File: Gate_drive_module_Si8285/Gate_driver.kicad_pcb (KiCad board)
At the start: 2 copper layers, 33 parts, among them J1 CONN_01X10, J2 CONN_01X04, J3 CONN_01X03, J4 CONN_01X03, J5 CONN_01X03, U1 Si8285, U2 Mornsun_QA01C

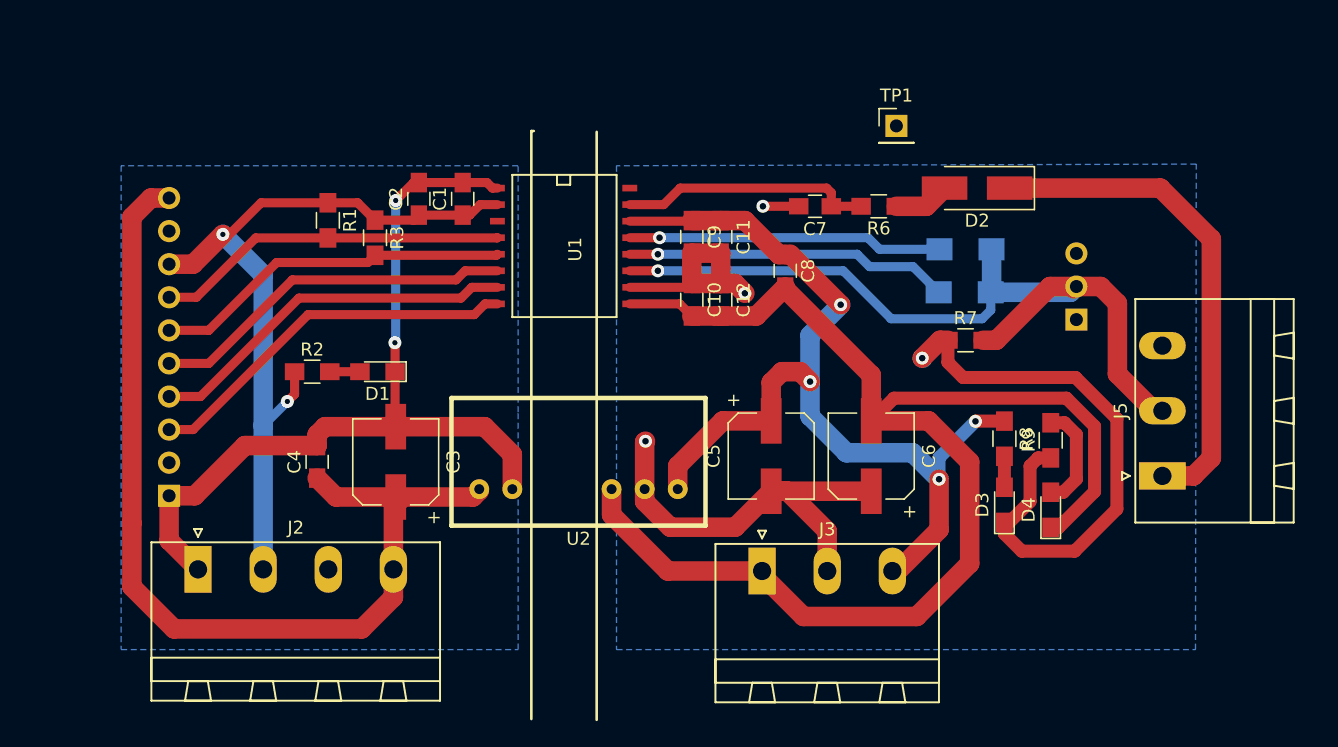
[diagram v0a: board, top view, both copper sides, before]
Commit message: Added edge cuts, logo, mounting holes, dimmensions, silkscreen
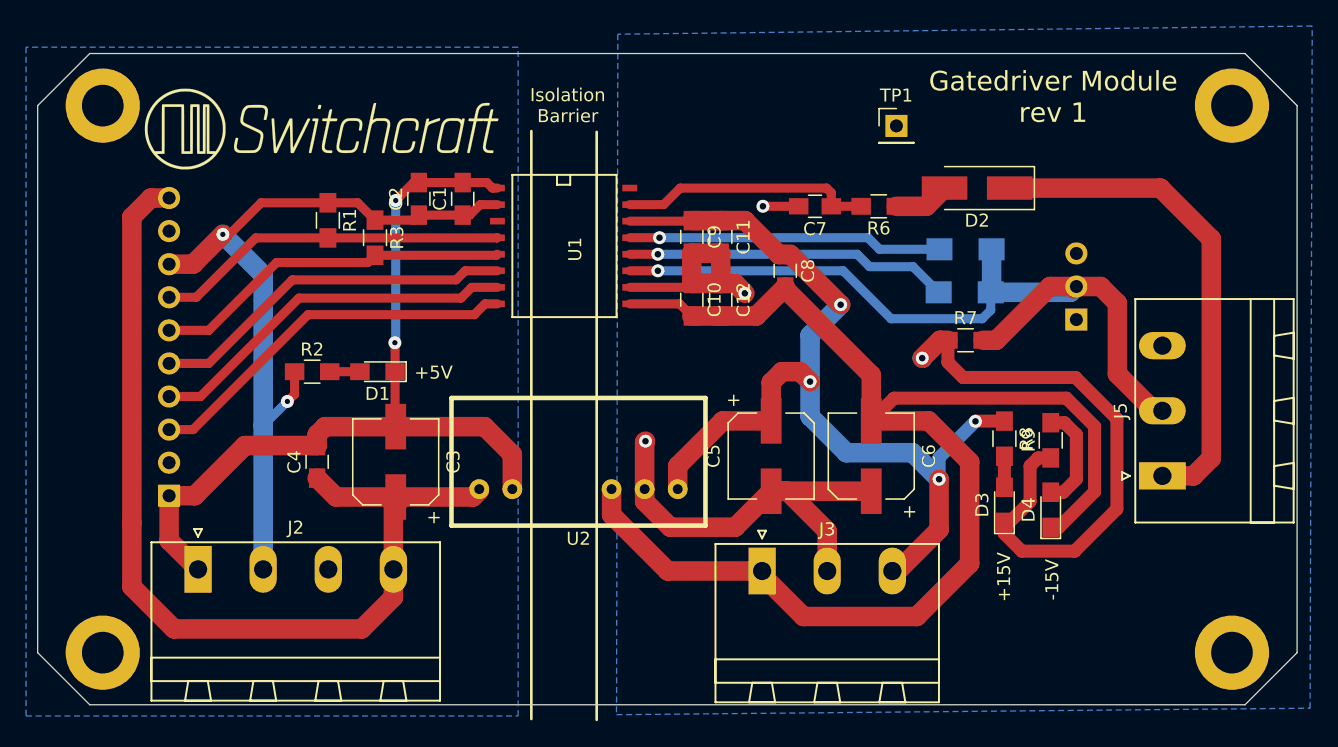
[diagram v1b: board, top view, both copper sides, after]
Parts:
- added G***: LOGO, Switchcraft:Switchcraft_medium_logo, F.Cu at (117.0, 111.8)
- added REF**: MountingHole_3.2mm_M3_ISO7380_Pad, Mounting_Holes:MountingHole_3.2mm_M3_ISO7380_Pad, F.Cu at (100.0, 110.0)
- added REF**: MountingHole_3.2mm_M3_ISO7380_Pad, Mounting_Holes:MountingHole_3.2mm_M3_ISO7380_Pad, F.Cu at (100.0, 152.0)
- added REF**: MountingHole_3.2mm_M3_ISO7380_Pad, Mounting_Holes:MountingHole_3.2mm_M3_ISO7380_Pad, F.Cu at (186.7, 110.0)
- added REF**: MountingHole_3.2mm_M3_ISO7380_Pad, Mounting_Holes:MountingHole_3.2mm_M3_ISO7380_Pad, F.Cu at (186.7, 152.0)
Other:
- board outline added: 96.7 x 50 mm
- board text added: "+15V"
- board text added: "+5V"
- board text added: "-15V"
- board text added: "Gatedriver Module rev 1"
- board text added: "Isolation Barrier"
- board text added: "Thou shall not pass"

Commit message: Added more measurements, adjusting screw holes
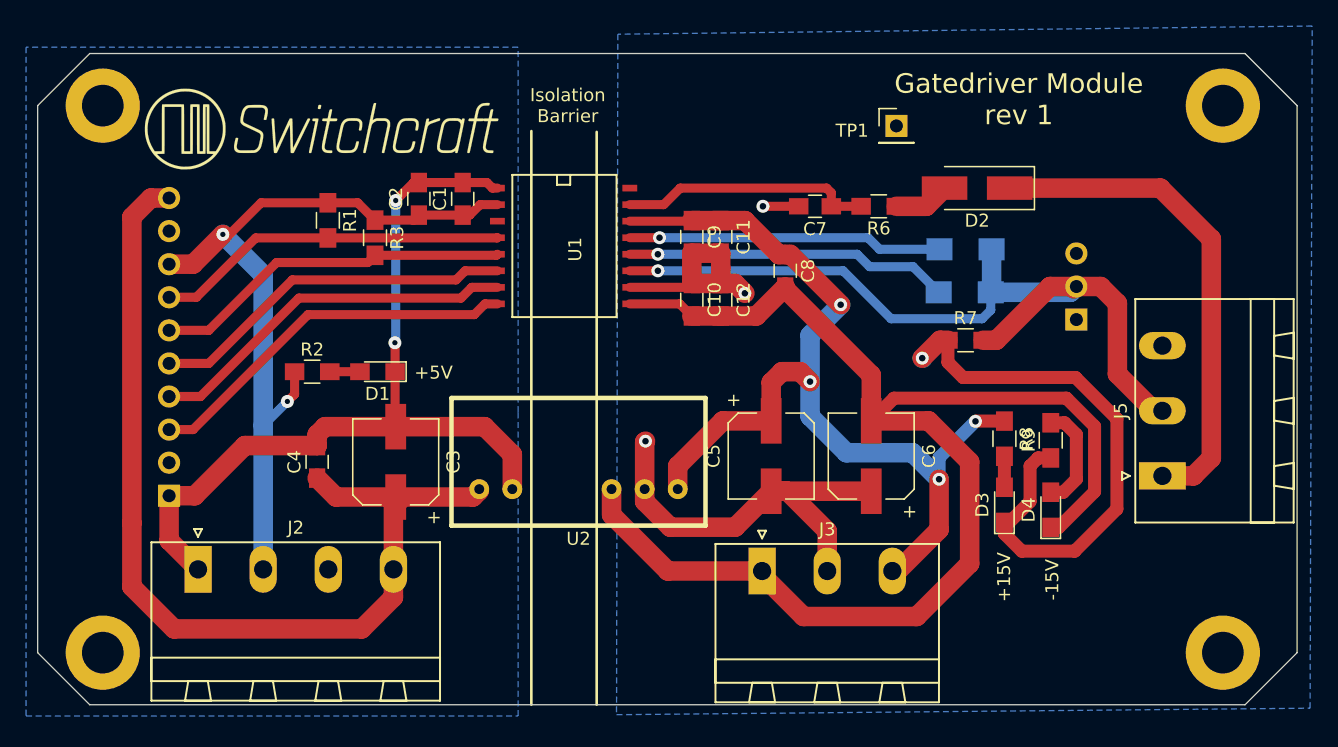
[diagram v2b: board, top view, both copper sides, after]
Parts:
- moved REF** 0.70 mm to (186.0, 110.0)
- moved REF** 0.70 mm to (186.0, 152.0)
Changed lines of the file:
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@@
     (area 94.949999 105.949999 191.750001 156.050001)
     (thickness 1.6)
-    (drawings 20)
+    (drawings 22)
     (tracks 240)
     (zones 0)
@@
     (pad_drill 0.6)
     (pad_to_mask_clearance 0)
-    (aux_axis_origin 0 0)
+    (aux_axis_origin 95 156)
+    (grid_origin 95 156)
     (visible_elements FFFFFF7F)
     (pcbplotparams
@@
     (descr "Through hole straight pin header, 1x01, 2.54mm pitch, single row")
     (tags "Through hole pin header THT 1x01 2.54mm single row")
-    (fp_text reference TP1 (at 0 -2.33) (layer F.SilkS)
+    (fp_text reference TP1 (at -3.4036 0.3683) (layer F.SilkS)
       (effects (font (size 1 1) (thickness 0.15)))
     )
@@
   )
   (module Mounting_Holes:MountingHole_3.2mm_M3_ISO7380_Pad (layer F.Cu)
-    (at 186.7 110)
+    (at 186 110)
     (descr "Mounting Hole 3.2mm, M3, ISO7380")
     (tags "mounting hole 3.2mm m3 iso7380")
@@
   )
   (module Mounting_Holes:MountingHole_3.2mm_M3_ISO7380_Pad (layer F.Cu)
-    (at 186.7 152)
+    (at 186 152)
     (descr "Mounting Hole 3.2mm, M3, ISO7380")
     (tags "mounting hole 3.2mm m3 iso7380")
@@
     (fp_circle (center 0 0) (end 3.1 0) (layer F.CrtYd) (width 0.05))
     (pad 1 thru_hole circle (at 0 0) (size 5.7 5.7) (drill 3.2) (layers *.Cu *.Mask))
+  )
+  (target plus (at 95 156) (size 5) (width 0.1) (layer Edge.Cuts))
+  (dimension 86 (width 0.3) (layer Dwgs.User)
+    (gr_text "86.000 mm" (at 143 161.35) (layer Dwgs.User)
+      (effects (font (size 1.5 1.5) (thickness 0.3)))
+    )
+    (feature1 (pts (xy 100 152) (xy 100 162.7)))
+    (feature2 (pts (xy 186 152) (xy 186 162.7)))
+    (crossbar (pts (xy 186 160) (xy 100 160)))
+    (arrow1a (pts (xy 100 160) (xy 101.126504 159.413579)))
+    (arrow1b (pts (xy 100 160) (xy 101.126504 160.586421)))
+    (arrow2a (pts (xy 186 160) (xy 184.873496 159.413579)))
+    (arrow2b (pts (xy 186 160) (xy 184.873496 160.586421)))
+  )
+  (dimension 69.578259 (width 0.3) (layer Dwgs.User)
+    (gr_text "69.578 mm" (at 139.984862 93.344091 359.939343) (layer Dwgs.User)
+      (effects (font (size 1.5 1.5) (thickness 0.3)))
+    )
+    (feature1 (pts (xy 105.16616 121.2596) (xy 105.197181 91.957262)))
+    (feature2 (pts (xy 174.74438 121.33326) (xy 174.775401 92.030922)))
+    (crossbar (pts (xy 174.772543 94.73092) (xy 105.194323 94.65726)))
+    (arrow1a (pts (xy 105.194323 94.65726) (xy 106.321447 94.072032)))
+    (arrow1b (pts (xy 105.194323 94.65726) (xy 106.320205 95.244873)))
+    (arrow2a (pts (xy 174.772543 94.73092) (xy 173.646661 94.143307)))
+    (arrow2b (pts (xy 174.772543 94.73092) (xy 173.645419 95.316148)))
   )
   (gr_text +5V (at 125.4 130.5) (layer F.SilkS)
@@
     (arrow2b (pts (xy 92.3 110) (xy 92.886421 111.126504)))
   )
-  (dimension 86.7 (width 0.3) (layer Dwgs.User)
-    (gr_text "86.700 mm" (at 143.35 163.25) (layer Dwgs.User)
-      (effects (font (size 1.5 1.5) (thickness 0.3)))
-    )
-    (feature1 (pts (xy 186.7 152) (xy 186.7 164.6)))
-    (feature2 (pts (xy 100 152) (xy 100 164.6)))
-    (crossbar (pts (xy 100 161.9) (xy 186.7 161.9)))
-    (arrow1a (pts (xy 186.7 161.9) (xy 185.573496 162.486421)))
-    (arrow1b (pts (xy 186.7 161.9) (xy 185.573496 161.313579)))
-    (arrow2a (pts (xy 100 161.9) (xy 101.126504 162.486421)))
-    (arrow2b (pts (xy 100 161.9) (xy 101.126504 161.313579)))
-  )
   (dimension 50.038 (width 0.3) (layer Dwgs.User)
     (gr_text "50.038 mm" (at 196.93 130.937 270) (layer Dwgs.User)
@@
     (effects (font (size 1 1) (thickness 0.2)))
   )
-  (gr_text "Gatedriver Module\nrev 1" (at 172.974 109.347) (layer F.SilkS)
+  (gr_text "Gatedriver Module\nrev 1" (at 170.3324 109.5248) (layer F.SilkS)
     (effects (font (size 1.5 1.5) (thickness 0.3)))
   )
@@
   (gr_line (start 95 152) (end 99 156) (angle 90) (layer Edge.Cuts) (width 0.1))
   (gr_line (start 95 110) (end 95 152) (angle 90) (layer Edge.Cuts) (width 0.1))
-  (gr_line (start 137.922 157.1625) (end 137.922 112.014) (angle 90) (layer F.SilkS) (width 0.2))
-  (gr_line (start 132.9055 157.099) (end 132.9055 111.9505) (angle 90) (layer F.SilkS) (width 0.2))
+  (gr_line (start 137.922 156) (end 137.922 112.014) (angle 90) (layer F.SilkS) (width 0.2))
+  (gr_line (start 132.9055 156) (end 132.9055 111.9505) (angle 90) (layer F.SilkS) (width 0.2))
   (segment (start 109.22 119.888) (end 112.315 122.983) (width 1.5) (layer B.Cu) (net 1))
   (via (at 109.22 119.888) (size 1) (drill 0.4) (layers F.Cu B.Cu) (net 1))
